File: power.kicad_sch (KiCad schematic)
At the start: 25 parts

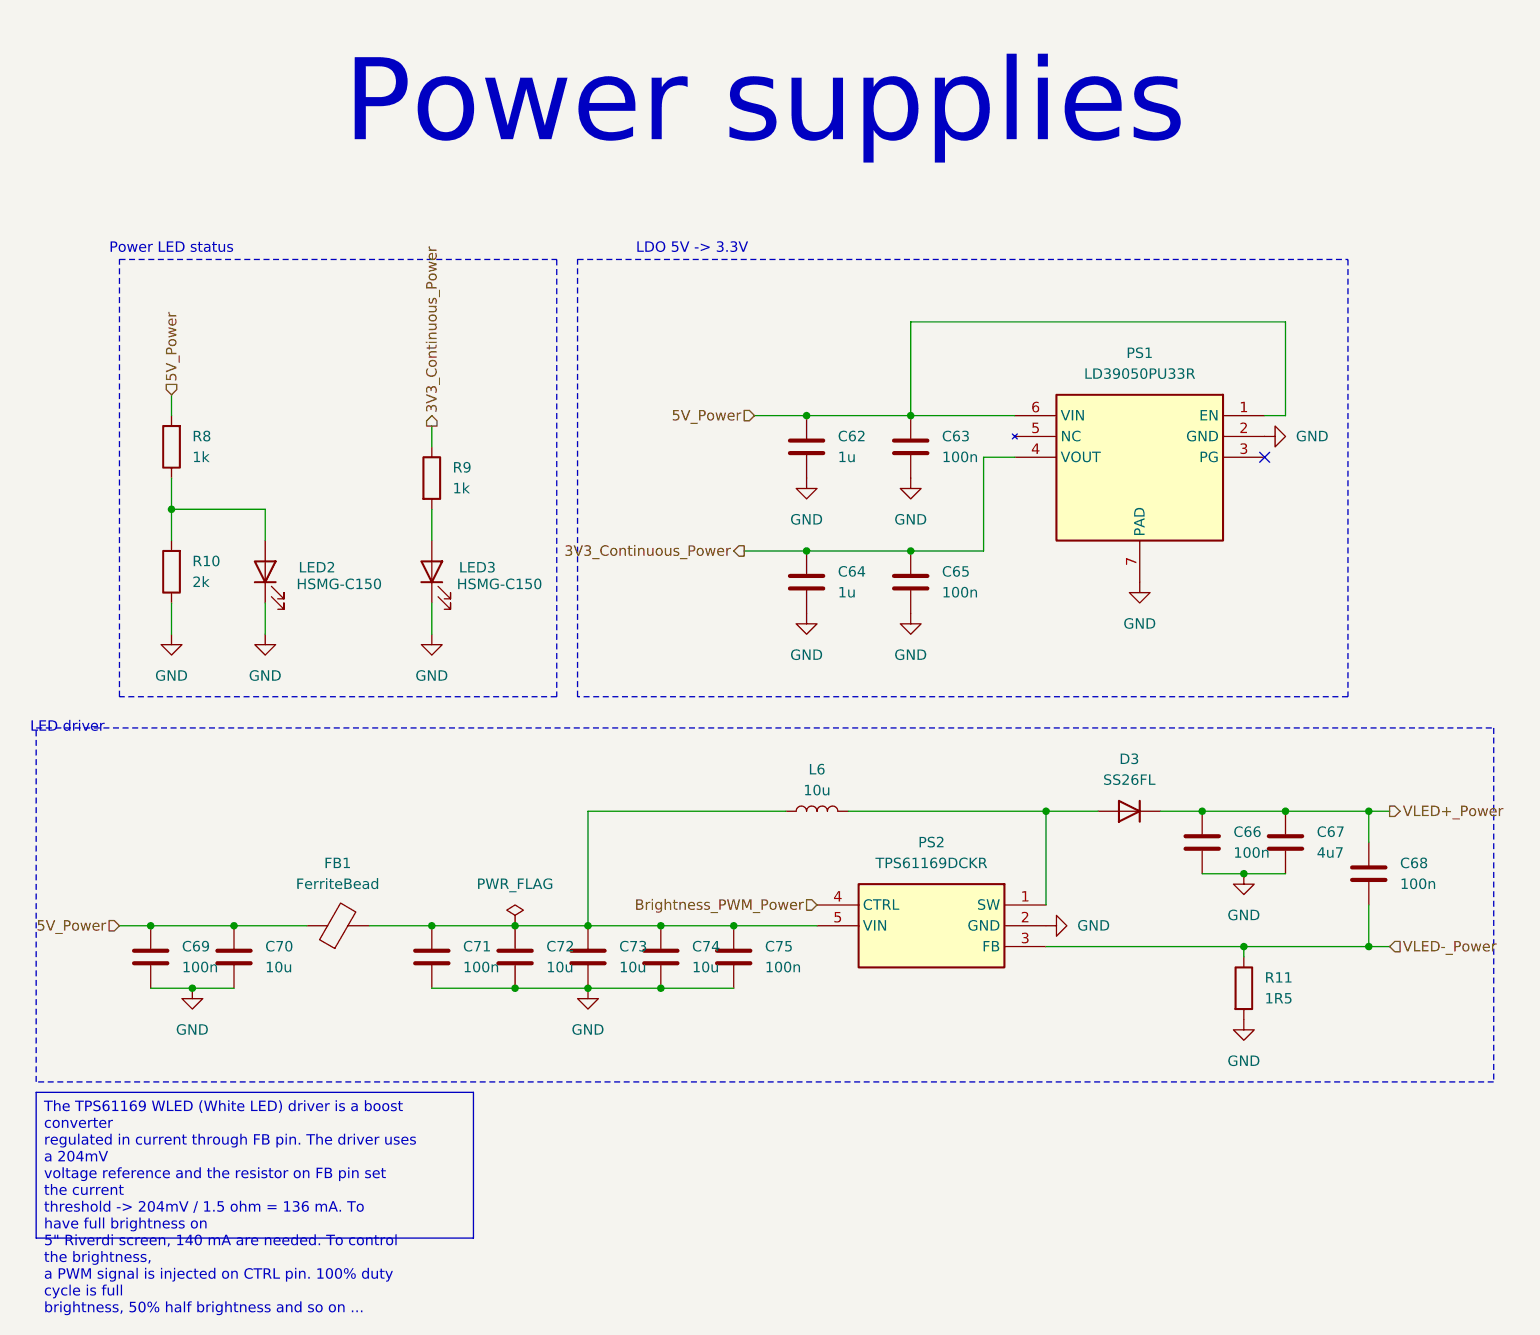
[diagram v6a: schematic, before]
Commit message: Place MCU and its components around
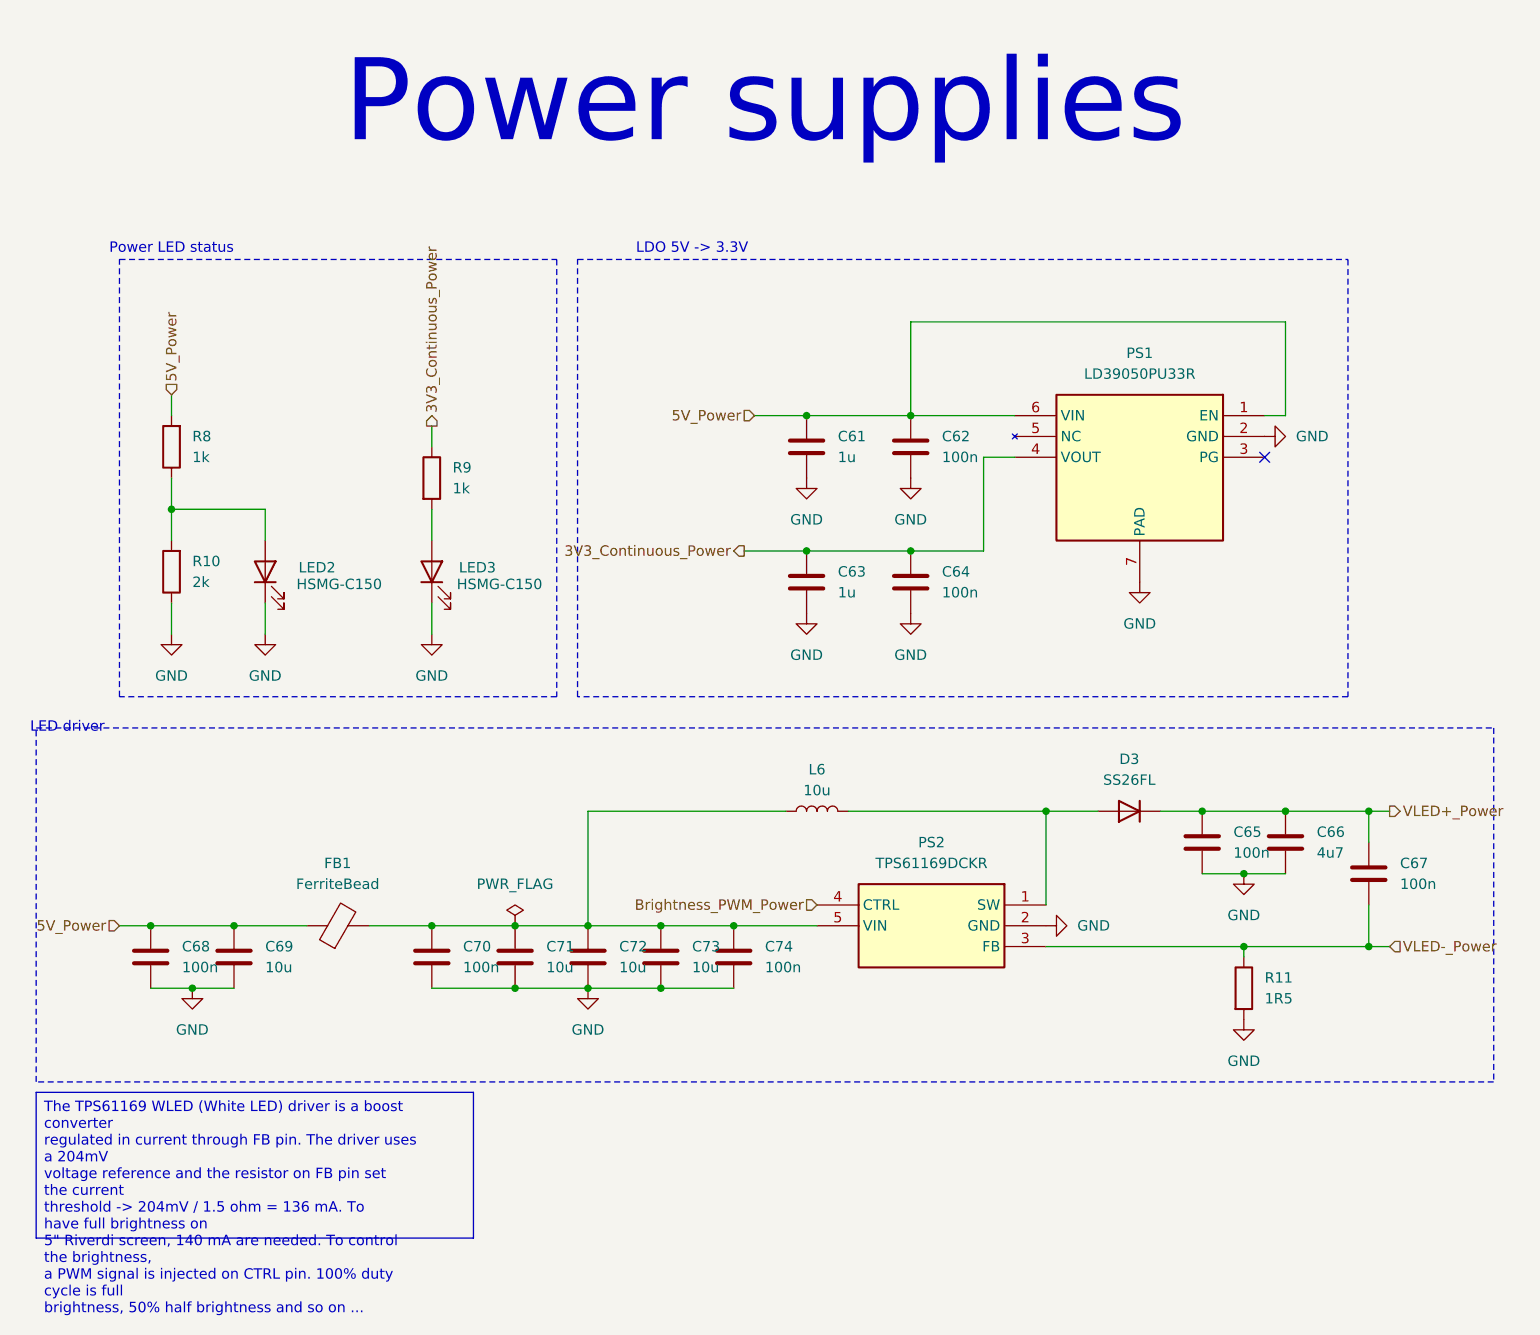
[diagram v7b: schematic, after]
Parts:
- renumbered C62 to C61, C63 to C62, C64 to C63, C65 to C64, C66 to C65, C67 to C66, C68 to C67, C69 to C68, C70 to C69, C71 to C70, C72 to C71, C73 to C72, C74 to C73, C75 to C74
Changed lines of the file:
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@@
 		(on_board yes)
 		(dnp no)
-		(property "Reference" "C66"
+		(property "Reference" "C65"
 			(at 210.82 113.0299 0)
 			(effects
@@
 			(project "weather-station-poc"
 				(path "/38eb53bb-294e-46e4-ad59-fd355ca373b9/12325ae0-3782-4eae-9f35-258d08cb4f7e"
-					(reference "C66")
+					(reference "C65")
 					(unit 1)
 				)
@@
 		(dnp no)
 		(fields_autoplaced yes)
-		(property "Reference" "#PWR0101"
+		(property "Reference" "#PWR0100"
 			(at 113.03 95.25 0)
 			(effects
@@
 			(project "weather-station-poc"
 				(path "/38eb53bb-294e-46e4-ad59-fd355ca373b9/12325ae0-3782-4eae-9f35-258d08cb4f7e"
-					(reference "#PWR0101")
+					(reference "#PWR0100")
 					(unit 1)
 				)
@@
 		(dnp no)
 		(fields_autoplaced yes)
-		(property "Reference" "#PWR0100"
+		(property "Reference" "#PWR099"
 			(at 92.71 95.25 0)
 			(effects
@@
 			(project "weather-station-poc"
 				(path "/38eb53bb-294e-46e4-ad59-fd355ca373b9/12325ae0-3782-4eae-9f35-258d08cb4f7e"
-					(reference "#PWR0100")
+					(reference "#PWR099")
 					(unit 1)
 				)
@@
 		(dnp no)
 		(fields_autoplaced yes)
-		(property "Reference" "#PWR098"
+		(property "Reference" "#PWR097"
 			(at 171.45 92.71 0)
 			(effects
@@
 			(project "weather-station-poc"
 				(path "/38eb53bb-294e-46e4-ad59-fd355ca373b9/12325ae0-3782-4eae-9f35-258d08cb4f7e"
-					(reference "#PWR098")
+					(reference "#PWR097")
 					(unit 1)
 				)
@@
 		(dnp no)
 		(fields_autoplaced yes)
-		(property "Reference" "#PWR095"
+		(property "Reference" "#PWR094"
 			(at 171.45 76.2 0)
 			(effects
@@
 			(project "weather-station-poc"
 				(path "/38eb53bb-294e-46e4-ad59-fd355ca373b9/12325ae0-3782-4eae-9f35-258d08cb4f7e"
-					(reference "#PWR095")
+					(reference "#PWR094")
 					(unit 1)
 				)
@@
 		(dnp no)
 		(fields_autoplaced yes)
-		(property "Reference" "C62"
+		(property "Reference" "C61"
 			(at 162.56 64.7699 0)
 			(effects
@@
 			(project ""
 				(path "/38eb53bb-294e-46e4-ad59-fd355ca373b9/12325ae0-3782-4eae-9f35-258d08cb4f7e"
-					(reference "C62")
+					(reference "C61")
 					(unit 1)
 				)
@@
 		(dnp no)
 		(fields_autoplaced yes)
-		(property "Reference" "C70"
+		(property "Reference" "C69"
 			(at 92.71 126.9999 0)
 			(effects
@@
 			(project "weather-station-poc"
 				(path "/38eb53bb-294e-46e4-ad59-fd355ca373b9/12325ae0-3782-4eae-9f35-258d08cb4f7e"
-					(reference "C70")
+					(reference "C69")
 					(unit 1)
 				)
@@
 		(dnp no)
 		(fields_autoplaced yes)
-		(property "Reference" "C69"
+		(property "Reference" "C68"
 			(at 82.55 126.9999 0)
 			(effects
@@
 			(project ""
 				(path "/38eb53bb-294e-46e4-ad59-fd355ca373b9/12325ae0-3782-4eae-9f35-258d08cb4f7e"
-					(reference "C69")
+					(reference "C68")
 					(unit 1)
 				)
@@
 		(dnp no)
 		(fields_autoplaced yes)
-		(property "Reference" "#PWR099"
+		(property "Reference" "#PWR098"
 			(at 81.28 95.25 0)
 			(effects
@@
 			(project "weather-station-poc"
 				(path "/38eb53bb-294e-46e4-ad59-fd355ca373b9/12325ae0-3782-4eae-9f35-258d08cb4f7e"
-					(reference "#PWR099")
+					(reference "#PWR098")
 					(unit 1)
 				)
@@
 		(dnp no)
 		(fields_autoplaced yes)
-		(property "Reference" "C75"
+		(property "Reference" "C74"
 			(at 153.67 126.9999 0)
 			(effects
@@
 			(project "weather-station-poc"
 				(path "/38eb53bb-294e-46e4-ad59-fd355ca373b9/12325ae0-3782-4eae-9f35-258d08cb4f7e"
-					(reference "C75")
+					(reference "C74")
 					(unit 1)
 				)
@@
 		(dnp no)
 		(fields_autoplaced yes)
-		(property "Reference" "#PWR0103"
+		(property "Reference" "#PWR0102"
 			(at 194.31 124.46 0)
 			(effects
@@
 			(project "weather-station-poc"
 				(path "/38eb53bb-294e-46e4-ad59-fd355ca373b9/12325ae0-3782-4eae-9f35-258d08cb4f7e"
-					(reference "#PWR0103")
+					(reference "#PWR0102")
 					(unit 1)
 				)
@@
 		(dnp no)
 		(fields_autoplaced yes)
-		(property "Reference" "#PWR096"
+		(property "Reference" "#PWR095"
 			(at 199.39 88.9 0)
 			(effects
@@
 			(project "weather-station-poc"
 				(path "/38eb53bb-294e-46e4-ad59-fd355ca373b9/12325ae0-3782-4eae-9f35-258d08cb4f7e"
-					(reference "#PWR096")
+					(reference "#PWR095")
 					(unit 1)
 				)
@@
 		(dnp no)
 		(fields_autoplaced yes)
-		(property "Reference" "#PWR094"
+		(property "Reference" "#PWR093"
 			(at 158.75 76.2 0)
 			(effects
@@
 			(project "weather-station-poc"
 				(path "/38eb53bb-294e-46e4-ad59-fd355ca373b9/12325ae0-3782-4eae-9f35-258d08cb4f7e"
-					(reference "#PWR094")
+					(reference "#PWR093")
 					(unit 1)
 				)
@@
 		(dnp no)
 		(fields_autoplaced yes)
-		(property "Reference" "C68"
+		(property "Reference" "C67"
 			(at 231.14 116.8399 0)
 			(effects
@@
 			(project "weather-station-poc"
 				(path "/38eb53bb-294e-46e4-ad59-fd355ca373b9/12325ae0-3782-4eae-9f35-258d08cb4f7e"
-					(reference "C68")
+					(reference "C67")
 					(unit 1)
 				)
@@
 		(dnp no)
 		(fields_autoplaced yes)
-		(property "Reference" "C64"
+		(property "Reference" "C63"
 			(at 162.56 81.2799 0)
 			(effects
@@
 			(project "weather-station-poc"
 				(path "/38eb53bb-294e-46e4-ad59-fd355ca373b9/12325ae0-3782-4eae-9f35-258d08cb4f7e"
-					(reference "C64")
+					(reference "C63")
 					(unit 1)
 				)
@@
 		(dnp no)
 		(fields_autoplaced yes)
-		(property "Reference" "C73"
+		(property "Reference" "C72"
 			(at 135.89 126.9999 0)
 			(effects
@@
 			(project "weather-station-poc"
 				(path "/38eb53bb-294e-46e4-ad59-fd355ca373b9/12325ae0-3782-4eae-9f35-258d08cb4f7e"
-					(reference "C73")
+					(reference "C72")
 					(unit 1)
 				)
@@
 		(dnp no)
 		(fields_autoplaced yes)
-		(property "Reference" "#PWR0102"
+		(property "Reference" "#PWR0101"
 			(at 212.09 124.46 0)
 			(effects
@@
 			(project "weather-station-poc"
 				(path "/38eb53bb-294e-46e4-ad59-fd355ca373b9/12325ae0-3782-4eae-9f35-258d08cb4f7e"
-					(reference "#PWR0102")
+					(reference "#PWR0101")
 					(unit 1)
 				)
@@
 		(dnp no)
 		(fields_autoplaced yes)
-		(property "Reference" "#PWR093"
+		(property "Reference" "#PWR092"
 			(at 220.98 64.77 0)
 			(effects
@@
 			(project "weather-station-poc"
 				(path "/38eb53bb-294e-46e4-ad59-fd355ca373b9/12325ae0-3782-4eae-9f35-258d08cb4f7e"
-					(reference "#PWR093")
+					(reference "#PWR092")
 					(unit 1)
 				)
@@
 		(dnp no)
 		(fields_autoplaced yes)
-		(property "Reference" "C65"
+		(property "Reference" "C64"
 			(at 175.26 81.2799 0)
 			(effects
@@
 			(project "weather-station-poc"
 				(path "/38eb53bb-294e-46e4-ad59-fd355ca373b9/12325ae0-3782-4eae-9f35-258d08cb4f7e"
-					(reference "C65")
+					(reference "C64")
 					(unit 1)
 				)
@@
 		(dnp no)
 		(fields_autoplaced yes)
-		(property "Reference" "C72"
+		(property "Reference" "C71"
 			(at 127 126.9999 0)
 			(effects
@@
 			(project "weather-station-poc"
 				(path "/38eb53bb-294e-46e4-ad59-fd355ca373b9/12325ae0-3782-4eae-9f35-258d08cb4f7e"
-					(reference "C72")
+					(reference "C71")
 					(unit 1)
 				)
@@
 		(dnp no)
 		(fields_autoplaced yes)
-		(property "Reference" "#PWR0104"
+		(property "Reference" "#PWR0103"
 			(at 83.82 138.43 0)
 			(effects
@@
 			(project ""
 				(path "/38eb53bb-294e-46e4-ad59-fd355ca373b9/12325ae0-3782-4eae-9f35-258d08cb4f7e"
-					(reference "#PWR0104")
+					(reference "#PWR0103")
 					(unit 1)
 				)
@@
 		(dnp no)
 		(fields_autoplaced yes)
-		(property "Reference" "#PWR097"
+		(property "Reference" "#PWR096"
 			(at 158.75 92.71 0)
 			(effects
@@
 			(project "weather-station-poc"
 				(path "/38eb53bb-294e-46e4-ad59-fd355ca373b9/12325ae0-3782-4eae-9f35-258d08cb4f7e"
-					(reference "#PWR097")
+					(reference "#PWR096")
 					(unit 1)
 				)
@@
 		(dnp no)
 		(fields_autoplaced yes)
-		(property "Reference" "C63"
+		(property "Reference" "C62"
 			(at 175.26 64.7699 0)
 			(effects
@@
 			(project "weather-station-poc"
 				(path "/38eb53bb-294e-46e4-ad59-fd355ca373b9/12325ae0-3782-4eae-9f35-258d08cb4f7e"
-					(reference "C63")
+					(reference "C62")
 					(unit 1)
 				)
@@
 		(dnp no)
 		(fields_autoplaced yes)
-		(property "Reference" "C74"
+		(property "Reference" "C73"
 			(at 144.78 126.9999 0)
 			(effects
@@
 			(project "weather-station-poc"
 				(path "/38eb53bb-294e-46e4-ad59-fd355ca373b9/12325ae0-3782-4eae-9f35-258d08cb4f7e"
-					(reference "C74")
+					(reference "C73")
 					(unit 1)
 				)
@@
 		(dnp no)
 		(fields_autoplaced yes)
-		(property "Reference" "C71"
+		(property "Reference" "C70"
 			(at 116.84 126.9999 0)
 			(effects
@@
 			(project "weather-station-poc"
 				(path "/38eb53bb-294e-46e4-ad59-fd355ca373b9/12325ae0-3782-4eae-9f35-258d08cb4f7e"
-					(reference "C71")
+					(reference "C70")
 					(unit 1)
 				)
@@
 		(dnp no)
 		(fields_autoplaced yes)
-		(property "Reference" "C67"
+		(property "Reference" "C66"
 			(at 220.98 113.0299 0)
 			(effects
@@
 			(project "weather-station-poc"
 				(path "/38eb53bb-294e-46e4-ad59-fd355ca373b9/12325ae0-3782-4eae-9f35-258d08cb4f7e"
-					(reference "C67")
+					(reference "C66")
 					(unit 1)
 				)
@@
 		(dnp no)
 		(fields_autoplaced yes)
-		(property "Reference" "#PWR0106"
+		(property "Reference" "#PWR0105"
 			(at 212.09 142.24 0)
 			(effects
@@
 			(project "weather-station-poc"
 				(path "/38eb53bb-294e-46e4-ad59-fd355ca373b9/12325ae0-3782-4eae-9f35-258d08cb4f7e"
-					(reference "#PWR0106")
+					(reference "#PWR0105")
 					(unit 1)
 				)
@@
 		(dnp no)
 		(fields_autoplaced yes)
-		(property "Reference" "#PWR0105"
+		(property "Reference" "#PWR0104"
 			(at 132.08 138.43 0)
 			(effects
@@
 			(project "weather-station-poc"
 				(path "/38eb53bb-294e-46e4-ad59-fd355ca373b9/12325ae0-3782-4eae-9f35-258d08cb4f7e"
-					(reference "#PWR0105")
-					(unit 1)
-				)
+					(reference "#PWR0104")
+					(unit 1)
+				)

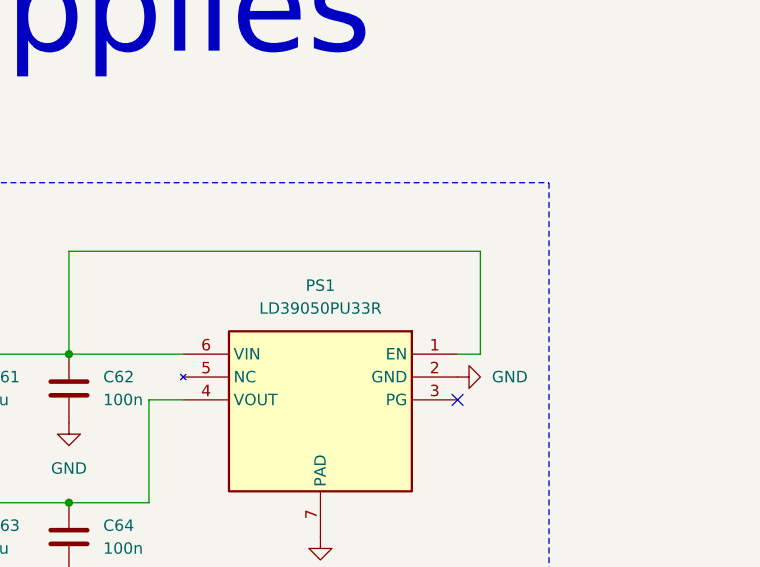
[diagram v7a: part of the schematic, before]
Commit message: Add ferrite bead part number in power schematic
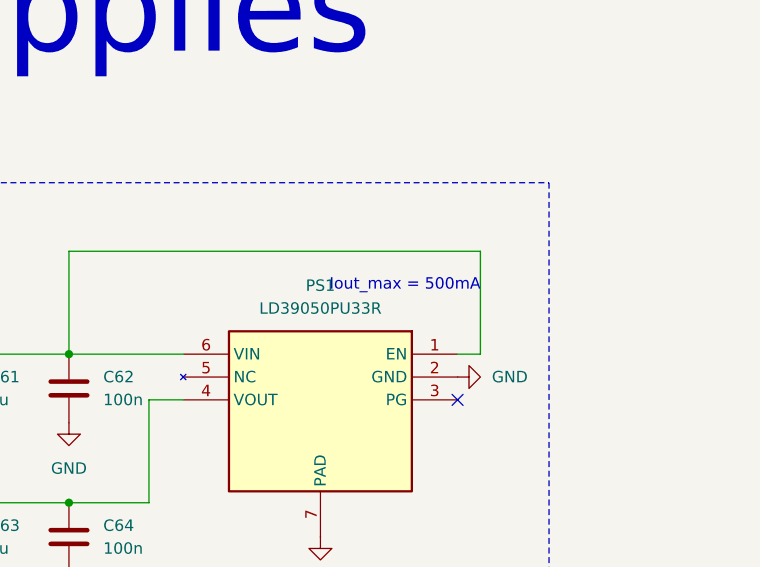
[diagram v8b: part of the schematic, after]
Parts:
- FB1: Part number (none) -> BLM18SG700TN1D
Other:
- note added: "Iout_max = 500mA"
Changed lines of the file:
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@@
+		)
+	)
+	(text "Iout_max = 500mA"
+		(exclude_from_sim no)
+		(at 208.788 54.61 0)
+		(effects
+			(font
+				(size 1.27 1.27)
+			)
 		)
 	)
@@
 			)
 		)
-		(property "Datasheet" "~"
+		(property "Datasheet" "https://www.mouser.fr/datasheet/3/76/1/ENFA0003.pdf"
 			(at 101.6 124.46 0)
 			(effects
@@
 			(effects
 				(font
+					(size 1.27 1.27)
+				)
+				(hide yes)
+			)
+		)
+		(property "Part number" "BLM18SG700TN1D"
+			(at 101.6 124.46 90)
+			(effects
+				(font
